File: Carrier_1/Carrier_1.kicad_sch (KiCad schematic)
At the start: 2 parts, among them J1 Chubut_2 connector, U1 LGAD_1_pad

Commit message: First version
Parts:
- added C1: 1n, Capacitor_SMD:C_1206_3216Metric_Pad1.33x1.80mm_HandSolder, symbol Device:C
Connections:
- net GND: now also C1.2
- net at J1.5 (Pin_5), U1.3: now also C1.1
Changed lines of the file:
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@@
 (kicad_sch (version 20211123) (generator eeschema)
   (paper "A4")
+  (junction (at 117.856 107.696) (diameter 0) (color 0 0 0 0)
+  )
   (wire (pts (xy 140.462 101.6) (xy 127.762 101.6))
     (stroke (width 0) (type default) (color 0 0 0 0))
@@
   (wire (pts (xy 117.856 107.696) (xy 117.856 102.87))
     (stroke (width 0) (type default) (color 0 0 0 0))
+  )
+  (symbol (lib_id "Device:C") (at 117.856 111.506 0) (unit 1)
+    (in_bom yes) (on_board yes)
+    (property "Reference" "C1" (id 0) (at 121.158 110.2359 0)
+      (effects (font (size 1.27 1.27)) (justify left))
+    )
+    (property "Value" "1n" (id 1) (at 121.158 112.7759 0)
+      (effects (font (size 1.27 1.27)) (justify left))
+    )
+    (property "Footprint" "Capacitor_SMD:C_1206_3216Metric_Pad1.33x1.80mm_HandSolder" (id 2) (at 118.8212 115.316 0)
+      (effects (font (size 1.27 1.27)) hide)
+    )
+    (property "Datasheet" "~" (id 3) (at 117.856 111.506 0)
+      (effects (font (size 1.27 1.27)) hide)
+    )
+    (property "Digikey" "https://www.digikey.ch/short/jfv8hn77" (id 4) (at 117.856 111.506 0)
+      (effects (font (size 1.27 1.27)) hide)
+    )
+    (property "Manufacturer number" "1206GC102KAT1A" (id 5) (at 129.286 115.062 0))
+    (property "Manufacturer" "KYOCERA AVX" (id 6) (at 117.856 111.506 0)
+      (effects (font (size 1.27 1.27)) hide)
+    )
+    (pin "1")
+    (pin "2")
+  )
+  (symbol (lib_id "power:GND") (at 117.856 115.316 0) (unit 1)
+    (in_bom yes) (on_board yes) (fields_autoplaced)
+    (property "Reference" "#PWR05" (id 0) (at 117.856 121.666 0)
+      (effects (font (size 1.27 1.27)) hide)
+    )
+    (property "Value" "GND" (id 1) (at 117.856 120.142 0))
+    (property "Footprint" "" (id 2) (at 117.856 115.316 0)
+      (effects (font (size 1.27 1.27)) hide)
+    )
+    (property "Datasheet" "" (id 3) (at 117.856 115.316 0)
+      (effects (font (size 1.27 1.27)) hide)
+    )
+    (pin "1")
   )
   (symbol (lib_id "Connector:Conn_01x05_Male") (at 145.542 96.52 0) (mirror y) (unit 1)
@@
       (reference "#PWR04") (unit 1) (value "GND") (footprint "")
     )
+    (path "/1485f178-70f5-424c-8e22-2eb40f551375"
+      (reference "#PWR05") (unit 1) (value "GND") (footprint "")
+    )
+    (path "/08435502-d1c5-4217-b63e-60d225d5c0e8"
+      (reference "C1") (unit 1) (value "1n") (footprint "Capacitor_SMD:C_1206_3216Metric_Pad1.33x1.80mm_HandSolder")
+    )
     (path "/1c9b814b-92c3-45f5-81f8-a7aa54755248"

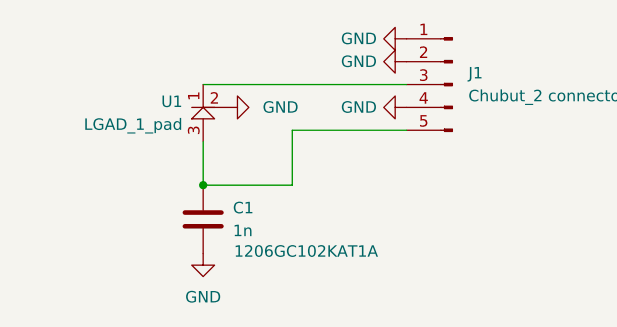
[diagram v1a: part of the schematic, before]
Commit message: Updated the carrier to be compatible with 2 pad devices
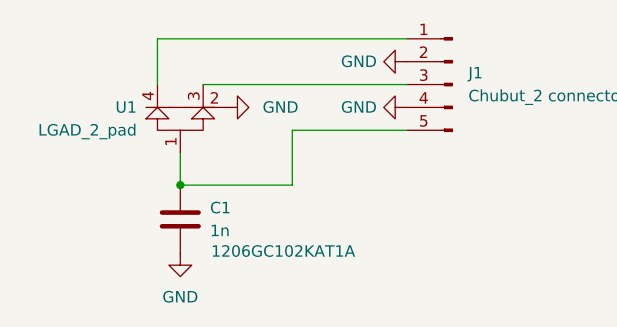
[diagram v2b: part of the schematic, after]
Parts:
- removed U1: LGAD_1_pad, chubut:LGAD, symbol LGAD:LGAD_1_pad
- added U1: LGAD_2_pad, chubut:LGAD, symbol LGAD:LGAD_2_pad
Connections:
- net GND: now also U1.2; no longer J1.1 (Pin_1)
- net at C1.1, J1.5 (Pin_5): now also U1.1
- net at J1.3 (Pin_3): now also U1.3
- new net: J1.1 (Pin_1), U1.4
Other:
- moved on the sheet: C1
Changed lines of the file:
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@@
 (kicad_sch (version 20211123) (generator eeschema)
   (paper "A4")
-  (junction (at 117.856 107.696) (diameter 0) (color 0 0 0 0)
+  (junction (at 115.316 107.696) (diameter 0) (color 0 0 0 0)
+  )
+  (wire (pts (xy 112.776 96.52) (xy 112.776 91.44))
+    (stroke (width 0) (type default) (color 0 0 0 0))
   )
   (wire (pts (xy 140.462 101.6) (xy 127.762 101.6))
     (stroke (width 0) (type default) (color 0 0 0 0))
   )
-  (wire (pts (xy 127.762 107.696) (xy 117.856 107.696))
+  (wire (pts (xy 112.776 91.44) (xy 140.462 91.44))
+    (stroke (width 0) (type default) (color 0 0 0 0))
+  )
+  (wire (pts (xy 127.762 107.696) (xy 115.316 107.696))
     (stroke (width 0) (type default) (color 0 0 0 0))
   )
@@
     (stroke (width 0) (type default) (color 0 0 0 0))
   )
-  (wire (pts (xy 117.856 107.696) (xy 117.856 102.87))
+  (wire (pts (xy 115.316 104.14) (xy 115.316 107.696))
     (stroke (width 0) (type default) (color 0 0 0 0))
   )
-  (symbol (lib_id "Device:C") (at 117.856 111.506 0) (unit 1)
+  (symbol (lib_id "Device:C") (at 115.316 111.506 0) (unit 1)
     (in_bom yes) (on_board yes)
-    (property "Reference" "C1" (id 0) (at 121.158 110.2359 0)
+    (property "Reference" "C1" (id 0) (at 118.618 110.2359 0)
       (effects (font (size 1.27 1.27)) (justify left))
     )
-    (property "Value" "1n" (id 1) (at 121.158 112.7759 0)
+    (property "Value" "1n" (id 1) (at 118.618 112.7759 0)
       (effects (font (size 1.27 1.27)) (justify left))
     )
-    (property "Footprint" "Capacitor_SMD:C_1206_3216Metric_Pad1.33x1.80mm_HandSolder" (id 2) (at 118.8212 115.316 0)
+    (property "Footprint" "Capacitor_SMD:C_1206_3216Metric_Pad1.33x1.80mm_HandSolder" (id 2) (at 116.2812 115.316 0)
       (effects (font (size 1.27 1.27)) hide)
     )
-    (property "Datasheet" "~" (id 3) (at 117.856 111.506 0)
+    (property "Datasheet" "~" (id 3) (at 115.316 111.506 0)
       (effects (font (size 1.27 1.27)) hide)
     )
-    (property "Digikey" "https://www.digikey.ch/short/jfv8hn77" (id 4) (at 117.856 111.506 0)
+    (property "Digikey" "https://www.digikey.ch/short/jfv8hn77" (id 4) (at 115.316 111.506 0)
       (effects (font (size 1.27 1.27)) hide)
     )
-    (property "Manufacturer number" "1206GC102KAT1A" (id 5) (at 129.286 115.062 0))
-    (property "Manufacturer" "KYOCERA AVX" (id 6) (at 117.856 111.506 0)
+    (property "Manufacturer number" "1206GC102KAT1A" (id 5) (at 126.746 115.062 0))
+    (property "Manufacturer" "KYOCERA AVX" (id 6) (at 115.316 111.506 0)
       (effects (font (size 1.27 1.27)) hide)
     )
@@
     (pin "2")
   )
-  (symbol (lib_id "power:GND") (at 117.856 115.316 0) (unit 1)
+  (symbol (lib_id "power:GND") (at 115.316 115.316 0) (unit 1)
     (in_bom yes) (on_board yes) (fields_autoplaced)
-    (property "Reference" "#PWR05" (id 0) (at 117.856 121.666 0)
+    (property "Reference" "#PWR01" (id 0) (at 115.316 121.666 0)
       (effects (font (size 1.27 1.27)) hide)
     )
-    (property "Value" "GND" (id 1) (at 117.856 120.142 0))
-    (property "Footprint" "" (id 2) (at 117.856 115.316 0)
+    (property "Value" "GND" (id 1) (at 115.316 120.142 0))
+    (property "Footprint" "" (id 2) (at 115.316 115.316 0)
       (effects (font (size 1.27 1.27)) hide)
     )
-    (property "Datasheet" "" (id 3) (at 117.856 115.316 0)
+    (property "Datasheet" "" (id 3) (at 115.316 115.316 0)
       (effects (font (size 1.27 1.27)) hide)
     )
@@
     (pin "5")
   )
-  (symbol (lib_id "power:GND") (at 140.462 91.44 270) (unit 1)
-    (in_bom yes) (on_board yes) (fields_autoplaced)
-    (property "Reference" "#PWR03" (id 0) (at 134.112 91.44 0)
-      (effects (font (size 1.27 1.27)) hide)
-    )
-    (property "Value" "GND" (id 1) (at 137.16 91.4399 90)
-      (effects (font (size 1.27 1.27)) (justify right))
-    )
-    (property "Footprint" "" (id 2) (at 140.462 91.44 0)
-      (effects (font (size 1.27 1.27)) hide)
-    )
-    (property "Datasheet" "" (id 3) (at 140.462 91.44 0)
-      (effects (font (size 1.27 1.27)) hide)
-    )
-    (pin "1")
-  )
-  (symbol (lib_id "LGAD:LGAD_1_pad") (at 117.856 96.52 0) (unit 1)
-    (in_bom yes) (on_board yes) (fields_autoplaced)
-    (property "Reference" "U1" (id 0) (at 115.57 98.4249 0)
-      (effects (font (size 1.27 1.27)) (justify right))
-    )
-    (property "Value" "LGAD_1_pad" (id 1) (at 115.57 100.9649 0)
-      (effects (font (size 1.27 1.27)) (justify right))
-    )
-    (property "Footprint" "chubut:LGAD" (id 2) (at 117.856 92.71 0)
-      (effects (font (size 1.27 1.27)) hide)
-    )
-    (property "Datasheet" "" (id 3) (at 117.856 92.71 0)
-      (effects (font (size 1.27 1.27)) hide)
-    )
-    (pin "1")
-    (pin "2")
-    (pin "3")
-  )
   (symbol (lib_id "power:GND") (at 120.396 99.06 90) (unit 1)
     (in_bom yes) (on_board yes) (fields_autoplaced)
-    (property "Reference" "#PWR01" (id 0) (at 126.746 99.06 0)
+    (property "Reference" "#PWR02" (id 0) (at 126.746 99.06 0)
       (effects (font (size 1.27 1.27)) hide)
     )
@@
     (pin "1")
   )
+  (symbol (lib_id "LGAD:LGAD_2_pad") (at 117.856 96.52 0) (unit 1)
+    (in_bom yes) (on_board yes) (fields_autoplaced)
+    (property "Reference" "U1" (id 0) (at 110.49 99.0599 0)
+      (effects (font (size 1.27 1.27)) (justify right))
+    )
+    (property "Value" "LGAD_2_pad" (id 1) (at 110.49 101.5999 0)
+      (effects (font (size 1.27 1.27)) (justify right))
+    )
+    (property "Footprint" "chubut:LGAD" (id 2) (at 117.856 92.71 0)
+      (effects (font (size 1.27 1.27)) hide)
+    )
+    (property "Datasheet" "" (id 3) (at 117.856 92.71 0)
+      (effects (font (size 1.27 1.27)) hide)
+    )
+    (pin "1")
+    (pin "2")
+    (pin "3")
+    (pin "4")
+  )
   (symbol (lib_id "power:GND") (at 140.462 93.98 270) (unit 1)
     (in_bom yes) (on_board yes) (fields_autoplaced)
-    (property "Reference" "#PWR02" (id 0) (at 134.112 93.98 0)
+    (property "Reference" "#PWR03" (id 0) (at 134.112 93.98 0)
       (effects (font (size 1.27 1.27)) hide)
     )
@@
   )
   (symbol_instances
-    (path "/8c1181af-4e79-4a34-8706-3c626984c028"
+    (path "/1485f178-70f5-424c-8e22-2eb40f551375"
       (reference "#PWR01") (unit 1) (value "GND") (footprint "")
     )
-    (path "/bb70edcb-85d3-4fa6-8a1b-953597a508c1"
+    (path "/8c1181af-4e79-4a34-8706-3c626984c028"
       (reference "#PWR02") (unit 1) (value "GND") (footprint "")
     )
-    (path "/336df69e-90e6-4f9a-b020-947ea24b77b6"
+    (path "/bb70edcb-85d3-4fa6-8a1b-953597a508c1"
       (reference "#PWR03") (unit 1) (value "GND") (footprint "")
     )
     (path "/d94212ff-7f9a-49cf-8573-2b36f1049727"
       (reference "#PWR04") (unit 1) (value "GND") (footprint "")
-    )
-    (path "/1485f178-70f5-424c-8e22-2eb40f551375"
-      (reference "#PWR05") (unit 1) (value "GND") (footprint "")
     )
     (path "/08435502-d1c5-4217-b63e-60d225d5c0e8"
@@
       (reference "J1") (unit 1) (value "Chubut_2 connector") (footprint "chubut:M22-5330505")
     )
-    (path "/448a26c2-1ef4-4286-bc0d-57c2c8f47307"
-      (reference "U1") (unit 1) (value "LGAD_1_pad") (footprint "chubut:LGAD")
+    (path "/a9e8be8f-71df-45ff-b93a-731421bc97ed"
+      (reference "U1") (unit 1) (value "LGAD_2_pad") (footprint "chubut:LGAD")
     )
   )

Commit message: Slight changes in the carrier board, added title, date, author to the pages
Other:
- company: (none) -> Universität Zürich
- title: (none) -> LGAD carrier board compatible with Chubut 2
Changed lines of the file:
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@@
 (kicad_sch (version 20211123) (generator eeschema)
   (paper "A4")
+  (title_block
+    (title "LGAD carrier board compatible with Chubut 2")
+    (date "2022-07-20")
+    (company "Universität Zürich")
+    (comment 1 "Matias Senger")
+  )
   (junction (at 115.316 107.696) (diameter 0) (color 0 0 0 0)
   )

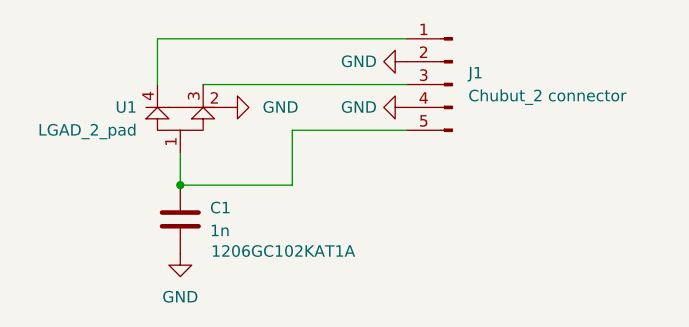
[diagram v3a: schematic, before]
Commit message: Design with spring loaded pins
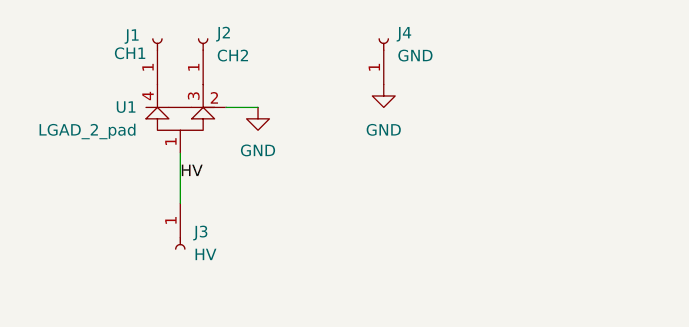
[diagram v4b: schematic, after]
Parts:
- removed C1: 1n, Capacitor_SMD:C_1206_3216Metric_Pad1.33x1.80mm_HandSolder, symbol Device:C
- removed J1: Chubut_2 connector, chubut:M22-5330505, symbol Connector:Conn_01x05_Male
- added J1: CH1, chubut:MILL-MAX_0965-0-15-20-80-14-11-0_contact, symbol Connector:Conn_01x01_Female
- added J2: CH2, chubut:MILL-MAX_0965-0-15-20-80-14-11-0_contact, symbol Connector:Conn_01x01_Female
- added J3: HV, chubut:MILL-MAX_0965-0-15-20-80-14-11-0_contact, symbol Connector:Conn_01x01_Female
- added J4: GND, chubut:MILL-MAX_0965-0-15-20-80-14-11-0_contact, symbol Connector:Conn_01x01_Female
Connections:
- net GND: now also J4.1 (Pin_1)
- net HV: now reaches U1.1
- net HV: now also J3.1 (Pin_1)
- net at U1.4: now also J1.1 (Pin_1)
- net at U1.3: now also J2.1 (Pin_1)

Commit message: Several updates
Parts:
- added H1, H2: MountingHole, MountingHole:MountingHole_2.1mm, symbol Mechanical:MountingHole
- renumbered J3 to J2, J2 to J3
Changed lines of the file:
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@@
     (comment 1 "Matias Senger")
   )
-  (wire (pts (xy 115.316 109.728) (xy 115.316 104.14))
+  (wire (pts (xy 115.316 104.14) (xy 115.316 109.728))
     (stroke (width 0) (type default) (color 0 0 0 0))
   )
@@
     (pin "1")
   )
+  (symbol (lib_id "Mechanical:MountingHole") (at 164.084 98.044 0) (unit 1)
+    (in_bom yes) (on_board yes) (fields_autoplaced)
+    (property "Reference" "H1" (id 0) (at 167.64 96.7739 0)
+      (effects (font (size 1.27 1.27)) (justify left))
+    )
+    (property "Value" "MountingHole" (id 1) (at 167.64 99.3139 0)
+      (effects (font (size 1.27 1.27)) (justify left))
+    )
+    (property "Footprint" "MountingHole:MountingHole_2.1mm" (id 2) (at 164.084 98.044 0)
+      (effects (font (size 1.27 1.27)) hide)
+    )
+    (property "Datasheet" "~" (id 3) (at 164.084 98.044 0)
+      (effects (font (size 1.27 1.27)) hide)
+    )
+  )
   (symbol (lib_id "Connector:Conn_01x01_Female") (at 115.316 114.808 270) (unit 1)
     (in_bom yes) (on_board yes) (fields_autoplaced)
-    (property "Reference" "J3" (id 0) (at 116.84 112.9029 90)
+    (property "Reference" "J2" (id 0) (at 116.84 112.9029 90)
       (effects (font (size 1.27 1.27)) (justify left))
     )
@@
     (pin "1")
   )
+  (symbol (lib_id "Mechanical:MountingHole") (at 164.084 104.902 0) (unit 1)
+    (in_bom yes) (on_board yes) (fields_autoplaced)
+    (property "Reference" "H2" (id 0) (at 167.64 103.6319 0)
+      (effects (font (size 1.27 1.27)) (justify left))
+    )
+    (property "Value" "MountingHole" (id 1) (at 167.64 106.1719 0)
+      (effects (font (size 1.27 1.27)) (justify left))
+    )
+    (property "Footprint" "MountingHole:MountingHole_2.1mm" (id 2) (at 164.084 104.902 0)
+      (effects (font (size 1.27 1.27)) hide)
+    )
+    (property "Datasheet" "~" (id 3) (at 164.084 104.902 0)
+      (effects (font (size 1.27 1.27)) hide)
+    )
+  )
   (symbol (lib_id "power:GND") (at 123.952 99.06 0) (unit 1)
     (in_bom yes) (on_board yes) (fields_autoplaced)
-    (property "Reference" "#PWR02" (id 0) (at 123.952 105.41 0)
+    (property "Reference" "#PWR01" (id 0) (at 123.952 105.41 0)
       (effects (font (size 1.27 1.27)) hide)
     )
@@
   (symbol (lib_id "Connector:Conn_01x01_Female") (at 117.856 91.44 90) (unit 1)
     (in_bom yes) (on_board yes) (fields_autoplaced)
-    (property "Reference" "J2" (id 0) (at 119.38 90.8049 90)
+    (property "Reference" "J3" (id 0) (at 119.38 90.8049 90)
       (effects (font (size 1.27 1.27)) (justify right))
     )
@@
   (symbol_instances
     (path "/8c1181af-4e79-4a34-8706-3c626984c028"
-      (reference "#PWR02") (unit 1) (value "GND") (footprint "")
+      (reference "#PWR01") (unit 1) (value "GND") (footprint "")
     )
     (path "/03d602b2-3255-4a87-8463-ecdd419c211c"
       (reference "#PWR03") (unit 1) (value "GND") (footprint "")
     )
+    (path "/062f7551-7233-45c7-81e7-06c638ae4e6a"
+      (reference "H1") (unit 1) (value "MountingHole") (footprint "MountingHole:MountingHole_2.1mm")
+    )
+    (path "/87df3fe7-ae00-46da-8148-53eb9a2a1c14"
+      (reference "H2") (unit 1) (value "MountingHole") (footprint "MountingHole:MountingHole_2.1mm")
+    )
     (path "/aa99d4a0-1ff7-40a7-a14b-5a17f52e7575"
       (reference "J1") (unit 1) (value "CH1") (footprint "chubut:MILL-MAX_0965-0-15-20-80-14-11-0_contact")
     )
+    (path "/76503ac6-17a0-42e3-968d-1d4bc53c1d29"
+      (reference "J2") (unit 1) (value "HV") (footprint "chubut:MILL-MAX_0965-0-15-20-80-14-11-0_contact")
+    )
     (path "/cbe69611-89ac-4760-8188-7237111fa6e5"
-      (reference "J2") (unit 1) (value "CH2") (footprint "chubut:MILL-MAX_0965-0-15-20-80-14-11-0_contact")
-    )
-    (path "/76503ac6-17a0-42e3-968d-1d4bc53c1d29"
-      (reference "J3") (unit 1) (value "HV") (footprint "chubut:MILL-MAX_0965-0-15-20-80-14-11-0_contact")
+      (reference "J3") (unit 1) (value "CH2") (footprint "chubut:MILL-MAX_0965-0-15-20-80-14-11-0_contact")
     )
     (path "/92cd58e5-fa23-485d-b6c8-39513f011369"

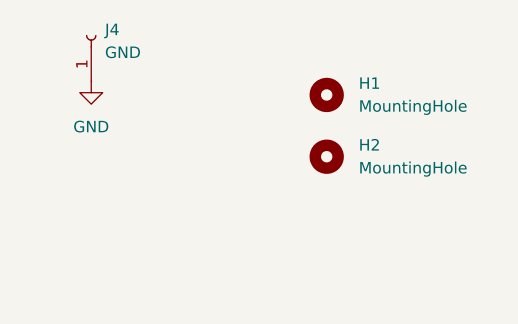
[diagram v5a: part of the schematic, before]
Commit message: Added mounting holes for testing different type of connection
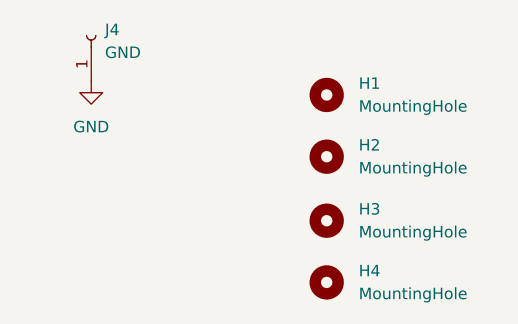
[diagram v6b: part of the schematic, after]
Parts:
- added H3, H4: MountingHole, MountingHole:MountingHole_2.1mm, symbol Mechanical:MountingHole
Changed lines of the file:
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@@
+    )
+  )
+  (symbol (lib_id "Mechanical:MountingHole") (at 164.084 118.872 0) (unit 1)
+    (in_bom yes) (on_board yes) (fields_autoplaced)
+    (property "Reference" "H4" (id 0) (at 167.64 117.6019 0)
+      (effects (font (size 1.27 1.27)) (justify left))
+    )
+    (property "Value" "MountingHole" (id 1) (at 167.64 120.1419 0)
+      (effects (font (size 1.27 1.27)) (justify left))
+    )
+    (property "Footprint" "MountingHole:MountingHole_2.1mm" (id 2) (at 164.084 118.872 0)
+      (effects (font (size 1.27 1.27)) hide)
+    )
+    (property "Datasheet" "~" (id 3) (at 164.084 118.872 0)
+      (effects (font (size 1.27 1.27)) hide)
     )
   )
@@
     (pin "1")
   )
+  (symbol (lib_id "Mechanical:MountingHole") (at 164.084 112.014 0) (unit 1)
+    (in_bom yes) (on_board yes) (fields_autoplaced)
+    (property "Reference" "H3" (id 0) (at 167.64 110.7439 0)
+      (effects (font (size 1.27 1.27)) (justify left))
+    )
+    (property "Value" "MountingHole" (id 1) (at 167.64 113.2839 0)
+      (effects (font (size 1.27 1.27)) (justify left))
+    )
+    (property "Footprint" "MountingHole:MountingHole_2.1mm" (id 2) (at 164.084 112.014 0)
+      (effects (font (size 1.27 1.27)) hide)
+    )
+    (property "Datasheet" "~" (id 3) (at 164.084 112.014 0)
+      (effects (font (size 1.27 1.27)) hide)
+    )
+  )
   (sheet_instances
     (path "/" (page "1"))
@@
       (reference "H2") (unit 1) (value "MountingHole") (footprint "MountingHole:MountingHole_2.1mm")
     )
+    (path "/fb646a8f-24ef-4fd2-b574-910a478e8381"
+      (reference "H3") (unit 1) (value "MountingHole") (footprint "MountingHole:MountingHole_2.1mm")
+    )
+    (path "/2c2a85a3-7cf2-4443-9b8b-7e9cd2b03f69"
+      (reference "H4") (unit 1) (value "MountingHole") (footprint "MountingHole:MountingHole_2.1mm")
+    )
     (path "/aa99d4a0-1ff7-40a7-a14b-5a17f52e7575"
